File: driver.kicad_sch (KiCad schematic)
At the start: 12 parts, among them U12 SN75107, U13 SN75110, U15 SN75110, U16 SN75110, U17 SN75110, U18 SN75110, U19 SN75110, U9 SN75107

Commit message: Aufnahme Schaltplan wip
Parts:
- added R10, R9: 470Ω, Resistor_THT:R_Axial_DIN0207_L6.3mm_D2.5mm_P7.62mm_Horizontal, symbol Device:R
- added RN10, RN11, RN2, RN3, RN5, RN6, RN7, RN8, RN9: 68Ω, Resistor_THT:R_Array_SIP6, symbol line termination resistors:3553
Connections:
- net at U9.11 (2B): now also R10.2
- net at U9.12 (2A): now also R9.2
- net SRV_CLK_TTL: now reaches U9.9 (2Y)
- new net SRV_CLK: R10.1
- new net /SRV_CLK: R9.1
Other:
- moved on the sheet: U9

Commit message: rev eng wip
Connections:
- net GND: now also RN5.1 (common), U19.1 (1A), U19.10 (D), U19.2 (1B), U19.3 (1C)
- net at U13.1 (1A): now also U13.2 (1B)
- net at U13.10 (D): now also U13.3 (1C), U13.4 (2C), U15.10 (D), U15.3 (1C), U15.4 (2C), U16.1 (1A), U16.10 (D), U16.4 (2C), U17.10 (D), U17.2 (1B), U17.3 (1C), U17.4 (2C), U17.5 (2A), U18.10 (D), U18.2 (1B), U18.3 (1C), U18.4 (2C), U18.5 (2A), U19.4 (2C)
- net at U13.5 (2A): now also U13.6 (2B)
- net LOAD_TTL___: now reaches U9.4 (1Y)
- net at RN5.2 (R1): now also U15.8 (2Y)
- net at RN5.3 (R2): now also U15.9 (2Z)
- net at RN5.5 (R3): now also U15.12 (1Z)
- net at RN5.6 (R4): now also U15.13 (1Y)
- net at U16.2 (1B): now also U16.3 (1C)
- net at U16.5 (2A): now also U16.6 (2B)
- net at U19.5 (2A): now also U19.6 (2B)
- net U5_QA: now reaches U15.1 (1A)
- net U5_QA: now also U15.2 (1B)
- net at U15.5 (2A): now also U15.6 (2B)
- net UNIT_SELECT_TTL: now reaches U12.4 (1Y)
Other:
- moved on the sheet: RN5, U18, U19

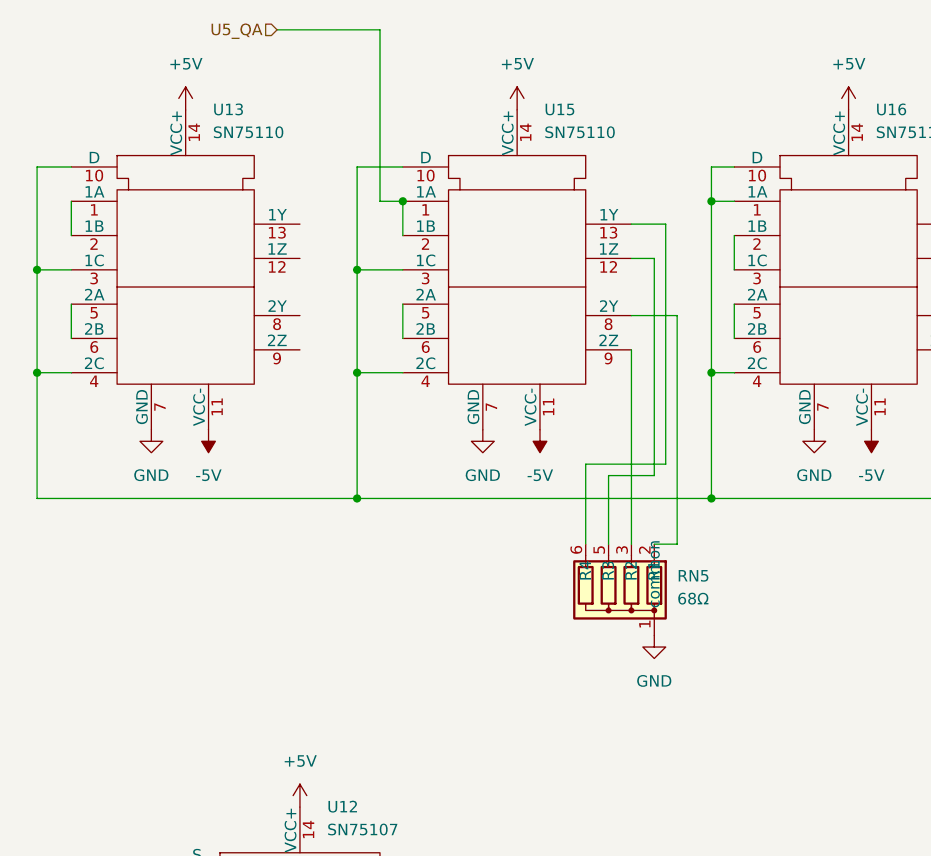
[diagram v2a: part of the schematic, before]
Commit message: Busses Names and more
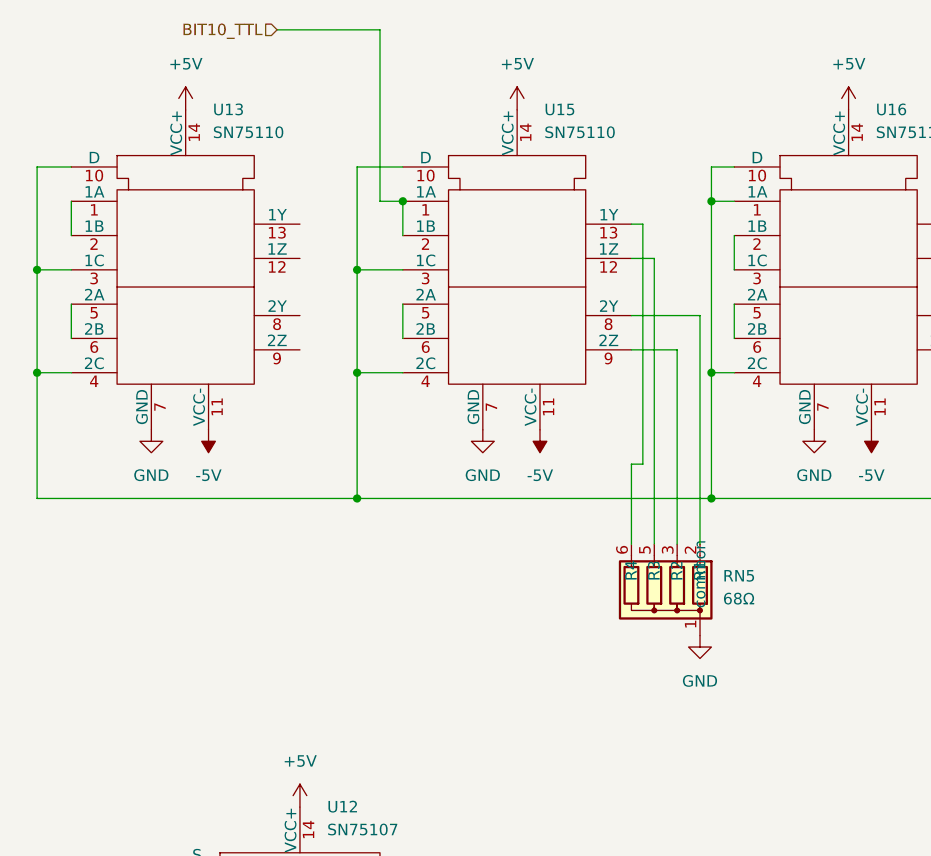
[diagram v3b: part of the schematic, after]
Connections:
- net U5_QA renamed BIT10_TTL
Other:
- moved on the sheet: RN5
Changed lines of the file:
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@@
 	(wire
 		(pts
-			(xy 109.22 43.18) (xy 109.22 67.31)
+			(xy 109.22 43.18) (xy 109.22 74.93)
 		)
 		(stroke
@@
 	(wire
 		(pts
-			(xy 101.6 66.04) (xy 101.6 74.93)
+			(xy 106.68 66.04) (xy 106.68 74.93)
 		)
 		(stroke
@@
 	(wire
 		(pts
-			(xy 111.76 74.93) (xy 109.22 74.93)
-		)
-		(stroke
-			(width 0)
-			(type default)
-		)
-	)
-	(wire
-		(pts
-			(xy 106.68 53.34) (xy 106.68 74.93)
-		)
-		(stroke
-			(width 0)
-			(type default)
-		)
-	)
-	(wire
-		(pts
 			(xy 81.28 44.45) (xy 76.2 44.45)
 		)
@@
 	(wire
 		(pts
-			(xy 106.68 39.37) (xy 110.49 39.37)
+			(xy 106.68 39.37) (xy 107.95 39.37)
 		)
 		(stroke
@@
 	(wire
 		(pts
-			(xy 111.76 49.53) (xy 111.76 74.93)
+			(xy 114.3 49.53) (xy 114.3 74.93)
 		)
 		(stroke
@@
 	(wire
 		(pts
-			(xy 110.49 66.04) (xy 101.6 66.04)
+			(xy 107.95 66.04) (xy 106.68 66.04)
 		)
 		(stroke
@@
 	(wire
 		(pts
-			(xy 54.61 121.92) (xy 55.88 121.92)
+			(xy 111.76 53.34) (xy 111.76 74.93)
 		)
 		(stroke
@@
 	(wire
 		(pts
-			(xy 81.28 33.02) (xy 76.2 33.02)
+			(xy 54.61 121.92) (xy 55.88 121.92)
 		)
 		(stroke
@@
 	(wire
 		(pts
-			(xy 109.22 67.31) (xy 104.14 67.31)
+			(xy 81.28 33.02) (xy 76.2 33.02)
 		)
 		(stroke
@@
 	(wire
 		(pts
-			(xy 110.49 39.37) (xy 110.49 66.04)
+			(xy 107.95 39.37) (xy 107.95 66.04)
 		)
 		(stroke
@@
 	(wire
 		(pts
-			(xy 106.68 49.53) (xy 111.76 49.53)
+			(xy 106.68 49.53) (xy 114.3 49.53)
 		)
 		(stroke
@@
 	(wire
 		(pts
-			(xy 104.14 67.31) (xy 104.14 74.93)
+			(xy 148.59 44.45) (xy 148.59 48.26)
 		)
 		(stroke
@@
 	(wire
 		(pts
-			(xy 148.59 44.45) (xy 148.59 48.26)
+			(xy 54.61 110.49) (xy 54.61 121.92)
 		)
 		(stroke
@@
 	(wire
 		(pts
-			(xy 54.61 110.49) (xy 54.61 121.92)
+			(xy 151.13 33.02) (xy 148.59 33.02)
 		)
 		(stroke
@@
 	(wire
 		(pts
-			(xy 151.13 33.02) (xy 148.59 33.02)
+			(xy 186.69 48.26) (xy 189.23 48.26)
 		)
 		(stroke
@@
 	(wire
 		(pts
-			(xy 186.69 48.26) (xy 189.23 48.26)
+			(xy 78.74 36.83) (xy 78.74 17.78)
 		)
 		(stroke
@@
 	(wire
 		(pts
-			(xy 78.74 36.83) (xy 78.74 17.78)
+			(xy 111.76 53.34) (xy 106.68 53.34)
 		)
 		(stroke
@@
 		)
 	)
-	(hierarchical_label "U5_QA"
+	(hierarchical_label "BIT10_TTL"
 		(shape input)
 		(at 67.31 17.78 180)
@@
 	(symbol
 		(lib_id "line termination resistors:3553")
-		(at 105.41 80.01 180)
+		(at 110.49 80.01 180)
 		(unit 1)
 		(exclude_from_sim no)
@@
 		(fields_autoplaced yes)
 		(property "Reference" "RN5"
-			(at 111.76 78.4859 0)
+			(at 116.84 78.4859 0)
 			(effects
 				(font
@@
 		)
 		(property "Value" "68Ω"
-			(at 111.76 81.0259 0)
+			(at 116.84 81.0259 0)
 			(effects
 				(font
@@
 		)
 		(property "Footprint" "Resistor_THT:R_Array_SIP6"
-			(at 105.156 66.548 0)
+			(at 110.236 66.548 0)
 			(effects
 				(font
@@
 		)
 		(property "Datasheet" ""
-			(at 105.41 80.01 0)
+			(at 110.49 80.01 0)
 			(effects
 				(font
@@
 		)
 		(property "Description" "Quad 68Ω Termination Resistors"
-			(at 104.902 64.516 0)
+			(at 109.982 64.516 0)
 			(effects
 				(font
@@
 	(symbol
 		(lib_id "power:GND")
-		(at 109.22 85.09 0)
+		(at 114.3 85.09 0)
 		(unit 1)
 		(exclude_from_sim no)
@@
 		(fields_autoplaced yes)
 		(property "Reference" "#PWR044"
-			(at 109.22 91.44 0)
+			(at 114.3 91.44 0)
 			(effects
 				(font
@@
 		)
 		(property "Value" "GND"
-			(at 109.22 90.17 0)
+			(at 114.3 90.17 0)
 			(effects
 				(font
@@
 		)
 		(property "Footprint" ""
-			(at 109.22 85.09 0)
+			(at 114.3 85.09 0)
 			(effects
 				(font
@@
 		)
 		(property "Datasheet" ""
-			(at 109.22 85.09 0)
+			(at 114.3 85.09 0)
 			(effects
 				(font
@@
 		)
 		(property "Description" "Power symbol creates a global label with name \"GND\" , ground"
-			(at 109.22 85.09 0)
+			(at 114.3 85.09 0)
 			(effects
 				(font

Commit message: weitere verdrahtungen nachvollzogen
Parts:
- added RN12: 68Ω, Resistor_THT:R_Array_SIP6, symbol line termination resistors:3553
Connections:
- net GND: now also RN6.1 (common), RN7.1 (common), RN8.1 (common), RN9.1 (common)
- net at RN9.2 (R1): now also U18.9 (2Z)
- net at RN9.3 (R2): now also U18.8 (2Y)
- net at RN9.5 (R3): now also U18.12 (1Z)
- net at RN9.6 (R4): now also U18.13 (1Y)
- net at RN8.2 (R1): now also U17.8 (2Y)
- net at RN8.3 (R2): now also U17.9 (2Z)
- net at RN8.5 (R3): now also U17.12 (1Z)
- net at RN8.6 (R4): now also U17.13 (1Y)
- net at U13.12 (1Z): now also RN5.2 (R1)
- net at U13.13 (1Y): now also RN5.3 (R2)
- net at U13.8 (2Y): now also RN5.6 (R4)
- net at U13.9 (2Z): now also RN5.5 (R3)
- net at U15.8 (2Y): now also RN6.2 (R1); no longer RN5.2 (R1)
- net at U15.9 (2Z): now also RN6.3 (R2); no longer RN5.3 (R2)
- net at U15.12 (1Z): now also RN6.5 (R3); no longer RN5.5 (R3)
- net at U15.13 (1Y): now also RN6.6 (R4); no longer RN5.6 (R4)
- net at U16.12 (1Z): now also RN7.5 (R3)
- net at U16.13 (1Y): now also RN7.6 (R4)
- net at U16.8 (2Y): now also RN7.3 (R2)
- net at U16.9 (2Z): now also RN7.2 (R1)
- net at U19.8 (2Y): now also RN10.5 (R3)
- net at U19.9 (2Z): now also RN10.6 (R4)
- no-connect marks 0 -> 2
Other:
- moved on the sheet: R4, R6, RN1, RN10, RN11, RN2, RN3, RN4, RN6, RN7, RN8, RN9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
